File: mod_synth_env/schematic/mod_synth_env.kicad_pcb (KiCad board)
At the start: 2 copper layers, 40.6 x 109.2 mm, 28 parts, among them J1 AudioJack2, J2 AudioJack2, J3 Conn_02x08_Odd_Even, J4 Conn_01x07_Female, J5 Conn_01x07_Male, SW1 SW_Push, SW2 SW_SPDT, U1 TL072

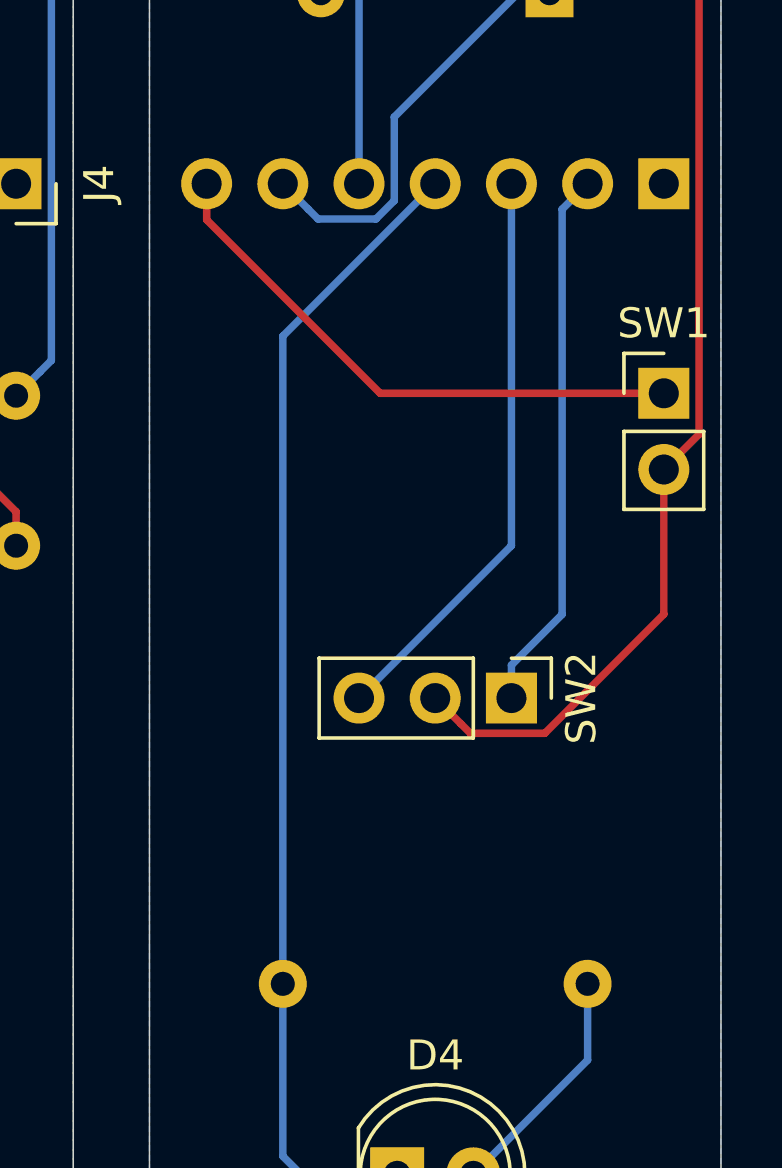
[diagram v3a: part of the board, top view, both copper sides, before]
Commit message: Add footprint for SPDT mini toggle switch
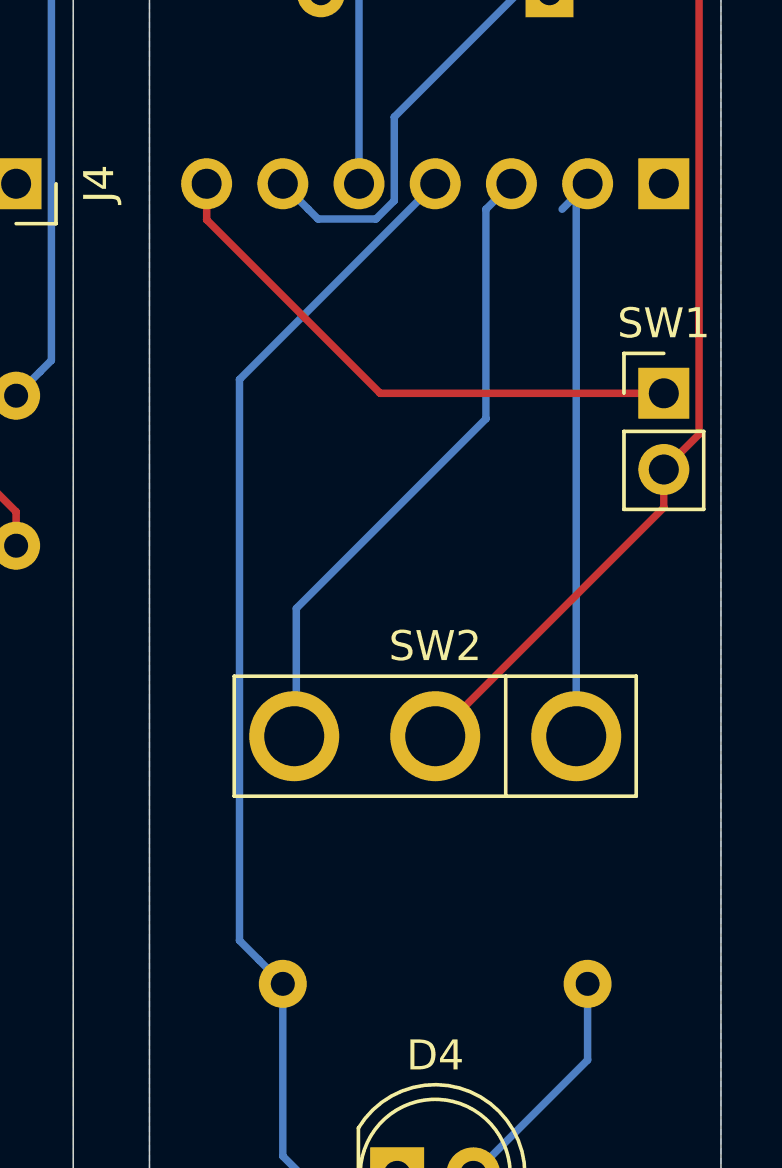
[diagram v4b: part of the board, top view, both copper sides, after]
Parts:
- SW2: footprint Connector_PinHeader_2.54mm:PinHeader_1x03_P2.54mm_Vertical -> mod_synth:Toggle-SPDT
- moved SW2 2.84 mm to (69.2, 103.5), turned to 180 degrees
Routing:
- net /GATE_IN_PCB_B: track 19.2 -> 21.4 mm
- net Net-(D3-Pad1): track 72.4 -> 70.3 mm
- net /TRIG_IN_PCB_B: track 18.2 -> 19.8 mm
- net /AMP_B_OUT_PCB_B: track 48.8 -> 50.0 mm
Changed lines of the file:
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@@
     (thickness 1.6)
     (drawings 8)
-    (tracks 126)
+    (tracks 127)
     (zones 0)
     (modules 28)
@@
     (add_net "Net-(U1-Pad8)")
   )
-  (module Connector_PinHeader_2.54mm:PinHeader_1x03_P2.54mm_Vertical (layer F.Cu)
-    (at 71.755 102.235 270)
-    (descr "Through hole straight pin header, 1x03, 2.54mm pitch, single row")
-    (tags "Through hole pin header THT 1x03 2.54mm single row")
-    (fp_text reference SW2 (at 0 -2.33 90) (layer F.SilkS)
-      (effects (font (size 1 1) (thickness 0.15)))
-    )
-    (fp_text value SW_SPDT (at 0 7.41 90) (layer F.Fab)
-      (effects (font (size 1 1) (thickness 0.15)))
-    )
-    (fp_text user %R (at 0 2.54) (layer F.Fab)
-      (effects (font (size 1 1) (thickness 0.15)))
-    )
-    (fp_line (start 1.8 -1.8) (end -1.8 -1.8) (layer F.CrtYd) (width 0.05))
-    (fp_line (start 1.8 6.85) (end 1.8 -1.8) (layer F.CrtYd) (width 0.05))
-    (fp_line (start -1.8 6.85) (end 1.8 6.85) (layer F.CrtYd) (width 0.05))
-    (fp_line (start -1.8 -1.8) (end -1.8 6.85) (layer F.CrtYd) (width 0.05))
-    (fp_line (start -1.33 -1.33) (end 0 -1.33) (layer F.SilkS) (width 0.12))
-    (fp_line (start -1.33 0) (end -1.33 -1.33) (layer F.SilkS) (width 0.12))
-    (fp_line (start -1.33 1.27) (end 1.33 1.27) (layer F.SilkS) (width 0.12))
-    (fp_line (start 1.33 1.27) (end 1.33 6.41) (layer F.SilkS) (width 0.12))
-    (fp_line (start -1.33 1.27) (end -1.33 6.41) (layer F.SilkS) (width 0.12))
-    (fp_line (start -1.33 6.41) (end 1.33 6.41) (layer F.SilkS) (width 0.12))
-    (fp_line (start -1.27 -0.635) (end -0.635 -1.27) (layer F.Fab) (width 0.1))
-    (fp_line (start -1.27 6.35) (end -1.27 -0.635) (layer F.Fab) (width 0.1))
-    (fp_line (start 1.27 6.35) (end -1.27 6.35) (layer F.Fab) (width 0.1))
-    (fp_line (start 1.27 -1.27) (end 1.27 6.35) (layer F.Fab) (width 0.1))
-    (fp_line (start -0.635 -1.27) (end 1.27 -1.27) (layer F.Fab) (width 0.1))
-    (pad 3 thru_hole oval (at 0 5.08 270) (size 1.7 1.7) (drill 1) (layers *.Cu *.Mask)
+  (module mod_synth:Toggle-SPDT (layer F.Cu)
+    (at 69.215 103.505 180)
+    (fp_text reference SW2 (at 0 3) (layer F.SilkS)
+      (effects (font (size 1 1) (thickness 0.15)))
+    )
+    (fp_text value SW_SPDT (at 0 -3) (layer F.Fab)
+      (effects (font (size 1 1) (thickness 0.15)))
+    )
+    (fp_line (start -6.45 1.75) (end -6.45 -1.75) (layer F.CrtYd) (width 0.05))
+    (fp_line (start 6.45 1.75) (end -6.45 1.75) (layer F.CrtYd) (width 0.05))
+    (fp_line (start 6.45 -1.75) (end 6.45 1.75) (layer F.CrtYd) (width 0.05))
+    (fp_line (start -6.45 -1.75) (end 6.45 -1.75) (layer F.CrtYd) (width 0.05))
+    (fp_line (start -2.35 -2) (end -2.35 2) (layer F.SilkS) (width 0.12))
+    (fp_line (start -6.7 2) (end -6.7 -2) (layer F.SilkS) (width 0.12))
+    (fp_line (start 6.7 2) (end -6.7 2) (layer F.SilkS) (width 0.12))
+    (fp_line (start 6.7 -2) (end 6.7 2) (layer F.SilkS) (width 0.12))
+    (fp_line (start -6.7 -2) (end 6.7 -2) (layer F.SilkS) (width 0.12))
+    (pad 3 thru_hole circle (at 4.7 0 180) (size 3 3) (drill 2) (layers *.Cu *.Mask)
       (net 30 /GATE_IN_PCB_B))
-    (pad 2 thru_hole oval (at 0 2.54 270) (size 1.7 1.7) (drill 1) (layers *.Cu *.Mask)
+    (pad 2 thru_hole circle (at 0 0 180) (size 3 3) (drill 2) (layers *.Cu *.Mask)
       (net 8 "Net-(D3-Pad1)"))
-    (pad 1 thru_hole rect (at 0 0 270) (size 1.7 1.7) (drill 1) (layers *.Cu *.Mask)
+    (pad 1 thru_hole circle (at -4.7 0 180) (size 3 3) (drill 2) (layers *.Cu *.Mask)
       (net 33 /TRIG_IN_PCB_B))
-    (model ${KISYS3DMOD}/Connector_PinHeader_2.54mm.3dshapes/PinHeader_1x03_P2.54mm_Vertical.wrl
-      (at (xyz 0 0 0))
-      (scale (xyz 1 1 1))
-      (rotate (xyz 0 0 0))
-    )
   )
   (module Connector_PinHeader_2.54mm:PinHeader_1x02_P2.54mm_Vertical (layer F.Cu)
@@
   (segment (start 78.010001 93.439999) (end 76.835 94.615) (width 0.25) (layer F.Cu) (net 8))
   (segment (start 78.010001 45.405001) (end 78.010001 93.439999) (width 0.25) (layer F.Cu) (net 8))
-  (segment (start 70.064999 103.084999) (end 69.215 102.235) (width 0.25) (layer F.Cu) (net 8))
   (segment (start 70.390001 103.410001) (end 70.064999 103.084999) (width 0.25) (layer F.Cu) (net 8))
-  (segment (start 72.865001 103.410001) (end 70.390001 103.410001) (width 0.25) (layer F.Cu) (net 8))
-  (segment (start 76.835 99.440002) (end 72.865001 103.410001) (width 0.25) (layer F.Cu) (net 8))
-  (segment (start 76.835 94.615) (end 76.835 99.440002) (width 0.25) (layer F.Cu) (net 8))
+  (segment (start 76.835 95.885) (end 69.215 103.505) (width 0.25) (layer F.Cu) (net 8))
+  (segment (start 76.835 94.615) (end 76.835 95.885) (width 0.25) (layer F.Cu) (net 8))
   (segment (start 74.295 114.3) (end 70.485 118.11) (width 0.25) (layer B.Cu) (net 9))
   (segment (start 74.295 111.76) (end 74.295 114.3) (width 0.25) (layer B.Cu) (net 9))
@@
   (segment (start 64.135 117.505) (end 64.135 111.76) (width 0.25) (layer B.Cu) (net 27))
   (segment (start 74.265 127.635) (end 64.135 117.505) (width 0.25) (layer B.Cu) (net 27))
-  (segment (start 64.135 90.17) (end 64.135 111.76) (width 0.25) (layer B.Cu) (net 27))
-  (segment (start 69.215 85.09) (end 64.135 90.17) (width 0.25) (layer B.Cu) (net 27))
+  (segment (start 63.335001 110.960001) (end 64.135 111.76) (width 0.25) (layer B.Cu) (net 27))
+  (segment (start 62.689999 110.314999) (end 63.335001 110.960001) (width 0.25) (layer B.Cu) (net 27))
+  (segment (start 62.689999 91.615001) (end 62.689999 110.314999) (width 0.25) (layer B.Cu) (net 27))
+  (segment (start 69.215 85.09) (end 62.689999 91.615001) (width 0.25) (layer B.Cu) (net 27))
   (segment (start 46.775001 84.240001) (end 47.625 85.09) (width 0.25) (layer F.Cu) (net 28))
   (segment (start 41.765001 79.230001) (end 46.775001 84.240001) (width 0.25) (layer F.Cu) (net 28))
@@
   (segment (start 47.625 44.45) (end 47.625 82.55) (width 0.25) (layer F.Cu) (net 29))
   (segment (start 45.085 41.91) (end 47.625 44.45) (width 0.25) (layer F.Cu) (net 29))
-  (segment (start 71.755 97.155) (end 66.675 102.235) (width 0.25) (layer B.Cu) (net 30))
-  (segment (start 71.755 85.09) (end 71.755 97.155) (width 0.25) (layer B.Cu) (net 30))
+  (segment (start 64.58501 99.24499) (end 64.58501 103.505) (width 0.25) (layer B.Cu) (net 30))
+  (segment (start 70.905001 92.924999) (end 64.58501 99.24499) (width 0.25) (layer B.Cu) (net 30))
+  (segment (start 71.755 85.09) (end 70.905001 85.939999) (width 0.25) (layer B.Cu) (net 30))
+  (segment (start 70.905001 85.939999) (end 70.905001 92.924999) (width 0.25) (layer B.Cu) (net 30))
   (segment (start 52.705 83.887919) (end 52.705 85.09) (width 0.25) (layer F.Cu) (net 32))
   (segment (start 52.705 47.864998) (end 52.705 83.887919) (width 0.25) (layer F.Cu) (net 32))
@@
   (segment (start 55.245 96.02363) (end 52.96001 93.73864) (width 0.25) (layer F.Cu) (net 32))
   (segment (start 55.245 97.155) (end 55.245 96.02363) (width 0.25) (layer F.Cu) (net 32))
-  (segment (start 71.755 101.135) (end 71.755 102.235) (width 0.25) (layer B.Cu) (net 33))
-  (segment (start 73.445001 99.444999) (end 71.755 101.135) (width 0.25) (layer B.Cu) (net 33))
-  (segment (start 73.445001 85.939999) (end 73.445001 99.444999) (width 0.25) (layer B.Cu) (net 33))
   (segment (start 74.295 85.09) (end 73.445001 85.939999) (width 0.25) (layer B.Cu) (net 33))
+  (segment (start 73.915 85.47) (end 74.295 85.09) (width 0.25) (layer B.Cu) (net 33))
+  (segment (start 73.915 103.505) (end 73.915 85.47) (width 0.25) (layer B.Cu) (net 33))
   (segment (start 76.16 92.075) (end 76.835 92.075) (width 0.25) (layer F.Cu) (net 34))
   (segment (start 67.377919 92.075) (end 76.16 92.075) (width 0.25) (layer F.Cu) (net 34))

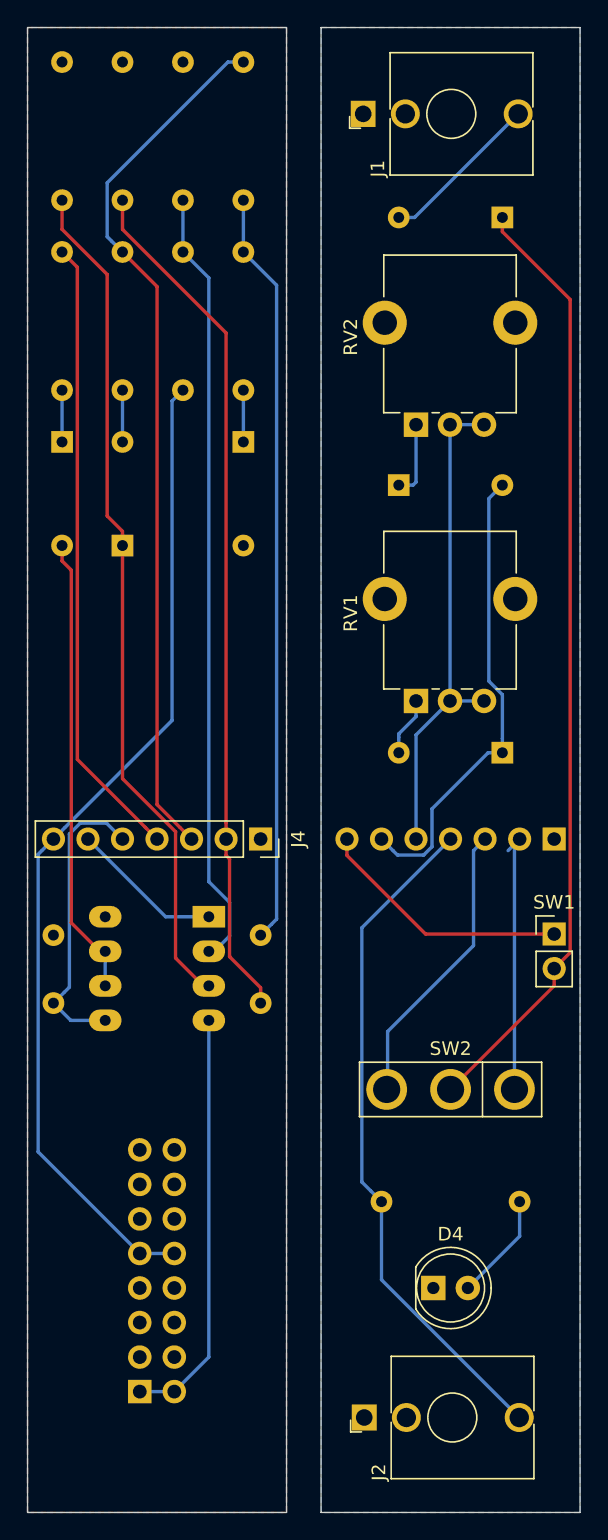
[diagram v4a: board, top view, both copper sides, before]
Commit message: Rework to add mounting point
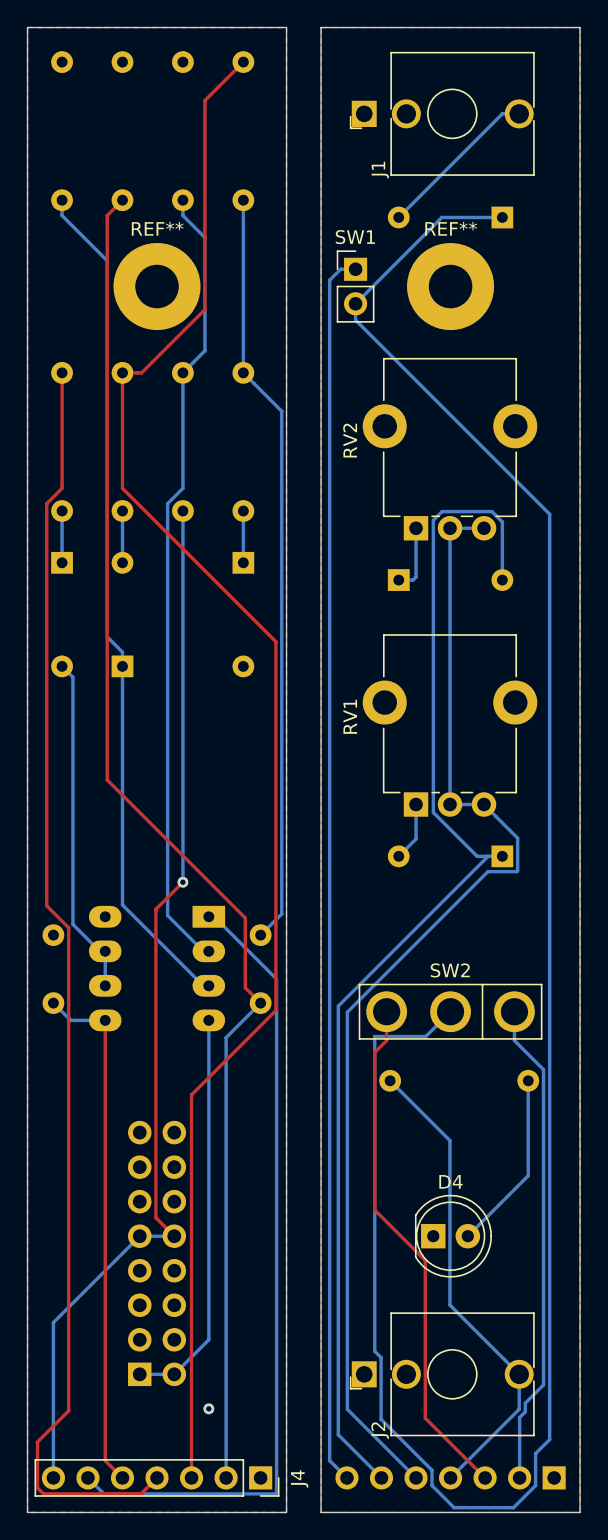
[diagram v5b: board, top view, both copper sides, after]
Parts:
- added REF**: MountingHole_3.2mm_M3_Pad, MountingHole:MountingHole_3.2mm_M3_Pad, F.Cu at (69.2, 44.5)
- added REF**: MountingHole_3.2mm_M3_Pad, MountingHole:MountingHole_3.2mm_M3_Pad, F.Cu at (47.6, 44.5)
- moved SW1 51.0 mm to (62.2, 43.2)
- moved J4 47.0 mm to (55.2, 132.1)
- moved J5 47.0 mm to (76.8, 132.1)
- moved R6 8.91 mm to (74.9, 102.9)
- moved D1 8.89 mm to (45.1, 72.4)
- moved R3 8.89 mm to (49.5, 50.8)
- moved R4 8.89 mm to (40.6, 61.0)
- moved R5 8.89 mm to (45.1, 50.8)
- moved R8 8.89 mm to (54.0, 61.0)
- moved D2 8.89 mm to (40.6, 64.8)
- moved D5 8.89 mm to (54.0, 64.8)
- moved D6 7.62 mm to (73.0, 86.4)
- moved RV2 7.62 mm to (66.7, 62.2)
- moved RV1 7.62 mm to (66.7, 82.5)
- moved D7 6.99 mm to (65.4, 66.0)
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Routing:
- net Net-(D3-Pad1): track 70.3 -> 156.8 mm
- net /+12_PCB_B: track 18.8 -> 90.9 mm
- net /AMP_A_OUT_PCB_B: track 34.6 -> 89.4 mm
- net /GATE_IN_PCB_A: track 64.5 -> 115.9 mm
- net /AMP_B_IN_PCB_B: track 36.5 -> 84.4 mm
- net /AMP_A_OUT_PCB_A: track 11.3 -> 59.1 mm
- net /AMP_B_OUT_PCB_A: track 46.1 -> 93.6 mm
- net /TRIG_IN_PCB_A: track 63.3 -> 100.2 mm
- net /GATE_IN_PCB_B: track 21.4 -> 38.0 mm
- net /AMP_B_IN_PCB_A: track 22.0 -> 38.5 mm
- net /TRIG_IN_PCB_B: track 19.8 -> 35.9 mm
- net /AMP_B_OUT_PCB_B: track 50.0 -> 35.2 mm
- net Net-(D2-Pad2): track 33.9 -> 25.0 mm
- net Net-(D4-Pad2): track 7.93 -> 13.3 mm
- net +12V: track 73.5 -> 77.7 mm, vias 0 -> 1
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- added copper zone on F.Cu, net /GND_PCB_B

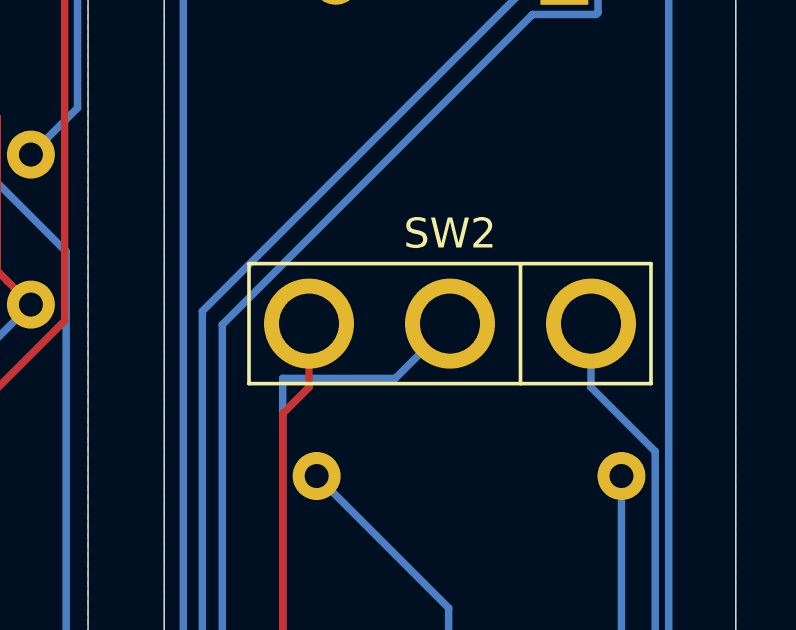
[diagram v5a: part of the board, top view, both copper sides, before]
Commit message: Update footprint for env
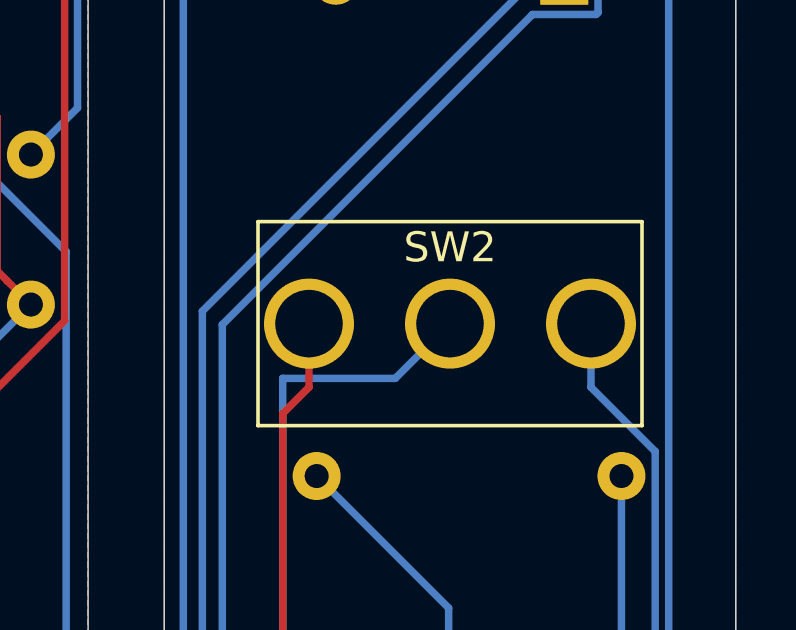
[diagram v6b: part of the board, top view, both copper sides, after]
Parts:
- SW2: footprint mod_synth:Toggle-SPDT -> mod_synth:SPDT_Switch_Vertical
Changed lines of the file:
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@@
     (add_net "Net-(U1-Pad8)")
+  )
+  (module mod_synth:SPDT_Switch_Vertical (layer F.Cu)
+    (at 69.215 97.79 180)
+    (fp_text reference SW2 (at 0 2.54) (layer F.SilkS)
+      (effects (font (size 1 1) (thickness 0.15)))
+    )
+    (fp_text value SW_SPDT (at 0 -2.286) (layer F.Fab)
+      (effects (font (size 1 1) (thickness 0.15)))
+    )
+    (fp_line (start -6.4 -3.4) (end 6.4 -3.4) (layer F.SilkS) (width 0.12))
+    (fp_line (start 6.4 3.4) (end 6.4 -3.4) (layer F.SilkS) (width 0.12))
+    (fp_line (start -6.4 3.4) (end 6.4 3.4) (layer F.SilkS) (width 0.12))
+    (fp_line (start -6.4 -3.4) (end -6.4 3.4) (layer F.SilkS) (width 0.12))
+    (pad 3 thru_hole circle (at 4.7 0 180) (size 3 3) (drill 2.25) (layers *.Cu *.Mask)
+      (net 30 /GATE_IN_PCB_B))
+    (pad 2 thru_hole circle (at 0 0 180) (size 3 3) (drill 2.25) (layers *.Cu *.Mask)
+      (net 8 "Net-(D3-Pad1)"))
+    (pad 1 thru_hole circle (at -4.7 0 180) (size 3 3) (drill 2.25) (layers *.Cu *.Mask)
+      (net 33 /TRIG_IN_PCB_B))
   )
   (module MountingHole:MountingHole_3.2mm_M3_Pad (layer F.Cu)
@@
     )
   )
-  (module mod_synth:Toggle-SPDT (layer F.Cu)
-    (at 69.215 97.79 180)
-    (fp_text reference SW2 (at 0 3) (layer F.SilkS)
-      (effects (font (size 1 1) (thickness 0.15)))
-    )
-    (fp_text value SW_SPDT (at 0 -3) (layer F.Fab)
-      (effects (font (size 1 1) (thickness 0.15)))
-    )
-    (fp_line (start -6.45 1.75) (end -6.45 -1.75) (layer F.CrtYd) (width 0.05))
-    (fp_line (start 6.45 1.75) (end -6.45 1.75) (layer F.CrtYd) (width 0.05))
-    (fp_line (start 6.45 -1.75) (end 6.45 1.75) (layer F.CrtYd) (width 0.05))
-    (fp_line (start -6.45 -1.75) (end 6.45 -1.75) (layer F.CrtYd) (width 0.05))
-    (fp_line (start -2.35 -2) (end -2.35 2) (layer F.SilkS) (width 0.12))
-    (fp_line (start -6.7 2) (end -6.7 -2) (layer F.SilkS) (width 0.12))
-    (fp_line (start 6.7 2) (end -6.7 2) (layer F.SilkS) (width 0.12))
-    (fp_line (start 6.7 -2) (end 6.7 2) (layer F.SilkS) (width 0.12))
-    (fp_line (start -6.7 -2) (end 6.7 -2) (layer F.SilkS) (width 0.12))
-    (pad 3 thru_hole circle (at 4.7 0 180) (size 3 3) (drill 2) (layers *.Cu *.Mask)
-      (net 30 /GATE_IN_PCB_B))
-    (pad 2 thru_hole circle (at 0 0 180) (size 3 3) (drill 2) (layers *.Cu *.Mask)
-      (net 8 "Net-(D3-Pad1)"))
-    (pad 1 thru_hole circle (at -4.7 0 180) (size 3 3) (drill 2) (layers *.Cu *.Mask)
-      (net 33 /TRIG_IN_PCB_B))
-  )
   (module Connector_PinHeader_2.54mm:PinHeader_1x02_P2.54mm_Vertical (layer F.Cu)
